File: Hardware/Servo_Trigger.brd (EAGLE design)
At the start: 20.3 x 38.1 mm, 21 parts, among them U1 ATTINY84, Y1 16MHZ

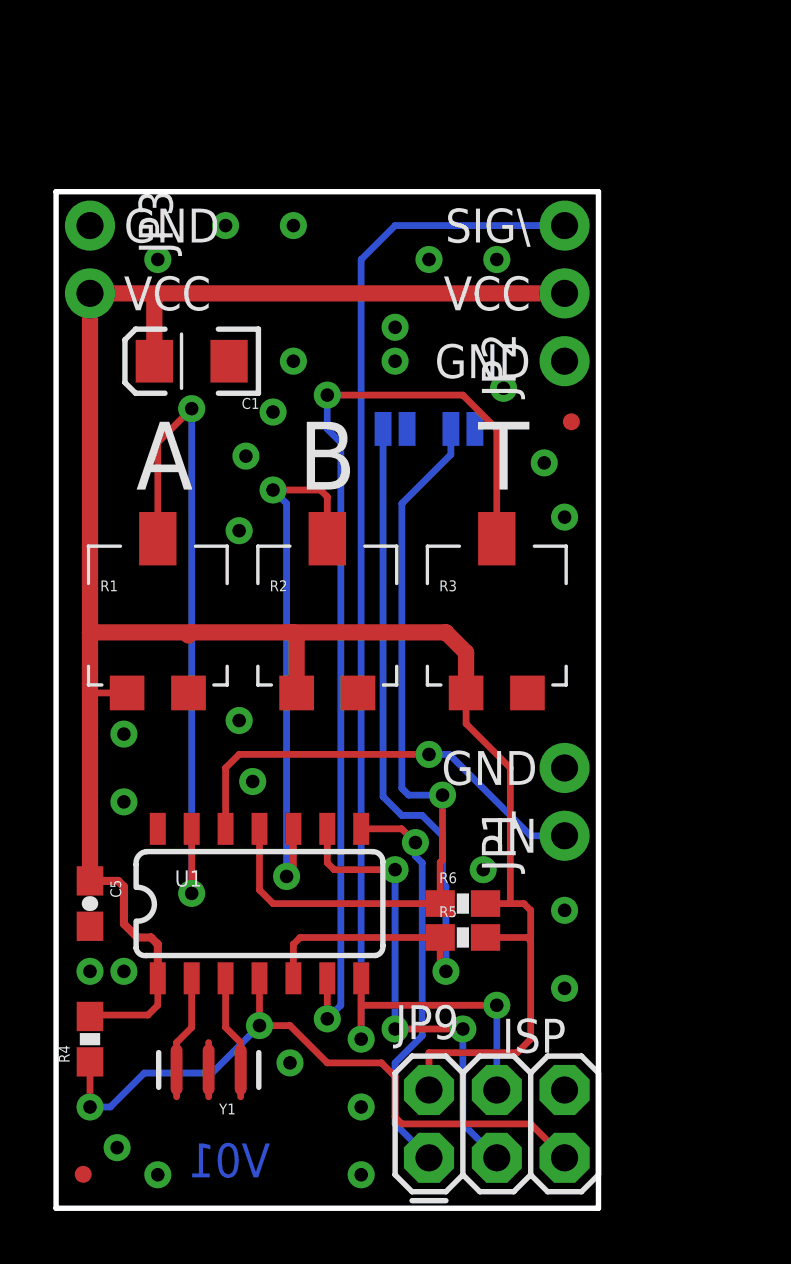
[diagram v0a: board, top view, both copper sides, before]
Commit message: Revision from collaborator and checklists
Added mounting holes, rearranged the interface connectors.
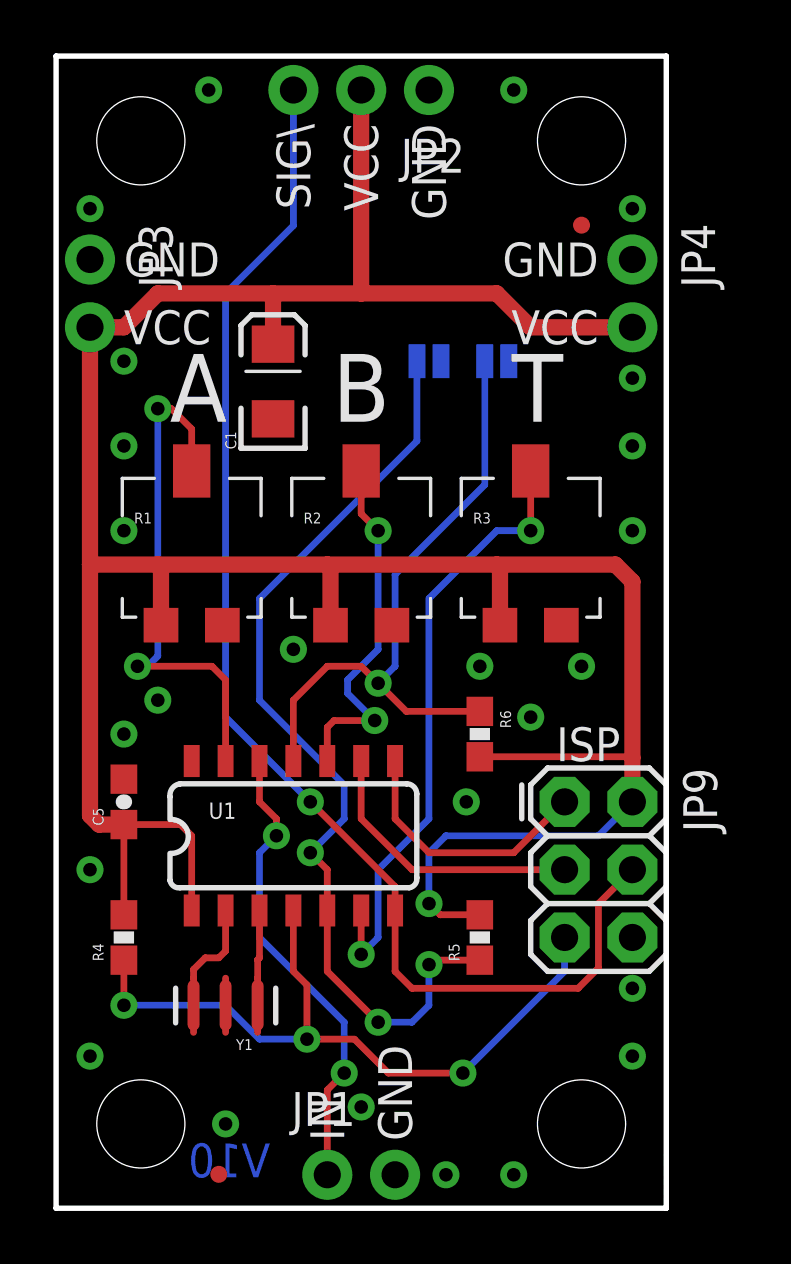
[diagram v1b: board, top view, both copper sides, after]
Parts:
- added JP4: M021X02_NO_SILK, SparkFun-Connectors:1X02_NO_SILK
- added STANDOFF1, STANDOFF2, STANDOFF3, STANDOFF4: STAND-OFF, SparkFun-Electromechanical:STAND-OFF
- R4, R5, R6: value 10k -> 10K
- moved JP1 15.5 mm to (10.2, 1.27), turned to 0 degrees
- moved JP9 14.3 mm to (19.1, 15.2), turned to 270 degrees
- moved JP2 11.4 mm to (14.0, 41.9), turned to 180 degrees
- moved FID2 7.38 mm to (19.7, 36.8)
- moved R6 6.38 mm to (15.9, 17.8), turned to 270 degrees
- moved FID1 5.08 mm to (6.10, 1.29)
- moved C5 4.02 mm to (2.54, 15.2), turned to 90 degrees
- moved R4 4.02 mm to (2.54, 10.2)
- moved C1 3.14 mm to (8.13, 31.0), turned to 90 degrees
- moved U1 2.84 mm to (8.89, 14.0)
- moved SJ1 2.84 mm to (14.0, 31.8)
- moved SJ2 2.84 mm to (16.5, 31.8)
- moved LOGO2 2.84 mm to (9.53, 31.8)
- moved R1 2.84 mm to (5.08, 24.4)
- moved R2 2.84 mm to (11.4, 24.4)
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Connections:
- net GND: now also JP4.1
- net VCC: now also JP4.2
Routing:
- net VCC: track 93.9 -> 113.4 mm, vias 0 -> 1
- net T: track 36.3 -> 23.1 mm
- net SCK: track 17.8 -> 10.6 mm, vias 3 -> 0
- net B: track 20.3 -> 13.7 mm
- net A: track 26.0 -> 19.9 mm
- net MODESEL: track 30.0 -> 35.8 mm, vias 1 -> 3
- net MISO: track 15.1 -> 9.83 mm, vias 1 -> 0
- net POLSEL: track 29.2 -> 24.2 mm
- net RESET: track 25.4 -> 27.1 mm, vias 2 -> 3
- net MOSI/PWM: track 47.9 -> 49.1 mm, vias 2 -> 1
- net BTN: track 16.5 -> 17.6 mm, vias 1 -> 2
- net N$4: track 2.64 -> 3.33 mm
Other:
- board size 20.3 x 38.1 mm -> 22.9 x 43.2 mm
- board text added: "V10"
- board text removed: "V01"
